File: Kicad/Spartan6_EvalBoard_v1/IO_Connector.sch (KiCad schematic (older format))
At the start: 14 parts, among them J201 CON2X45

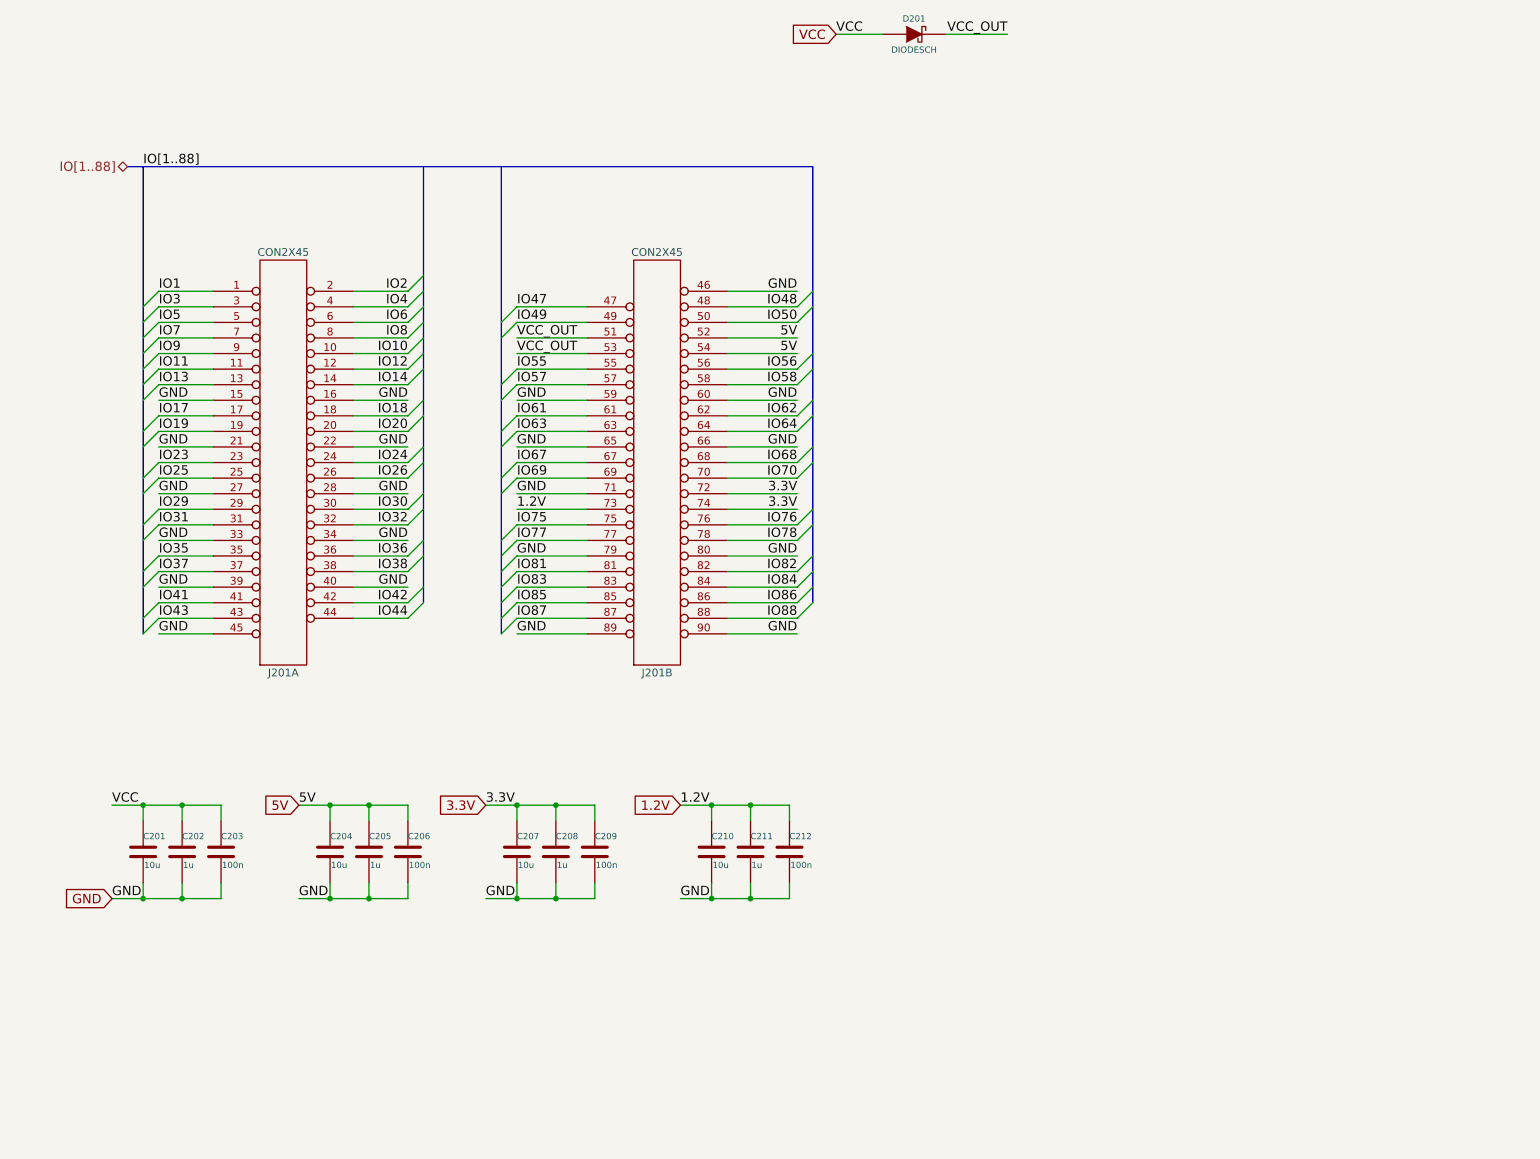
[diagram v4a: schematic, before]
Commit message: Layout completed, just need to run DRC.
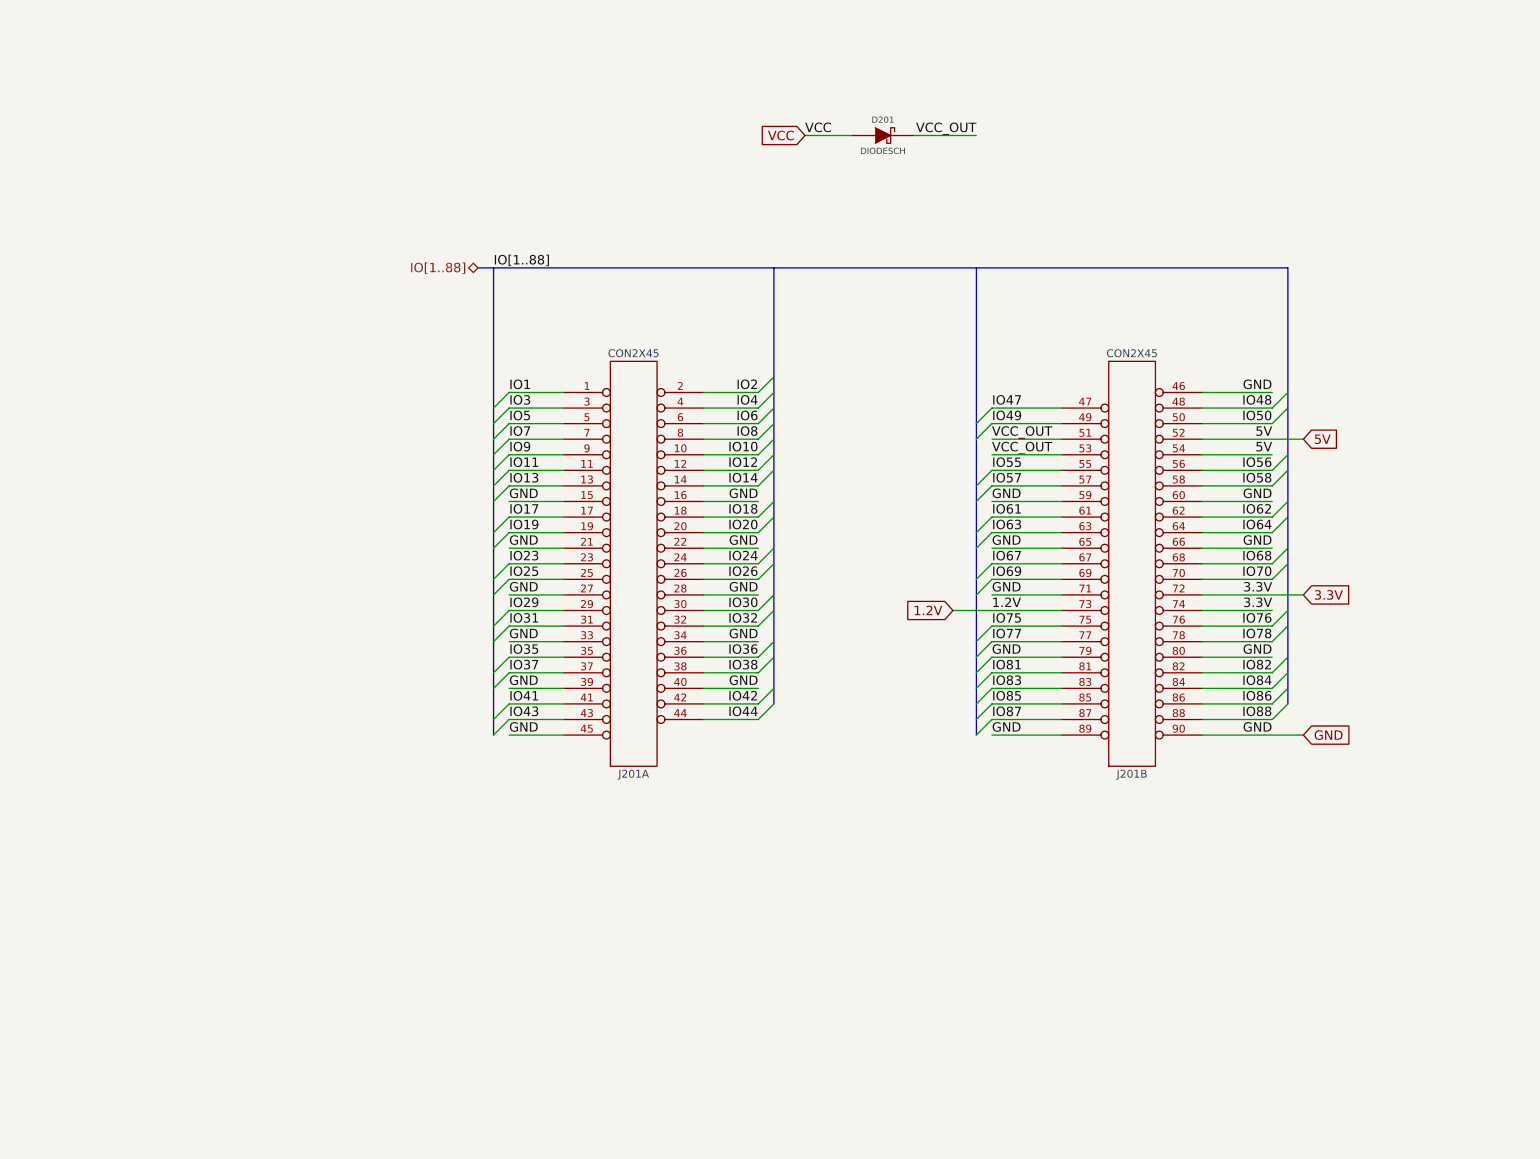
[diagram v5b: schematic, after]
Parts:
- removed C201, C204, C207, C210: 10u, Capacitors_SMD.pretty:C_0603, symbol C
- removed C202, C205, C208, C211: 1u, Capacitors_SMD.pretty:C_0402, symbol C
- removed C203, C206, C209, C212: 100n, Capacitors_SMD.pretty:C_0402, symbol C
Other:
- moved on the sheet: D201, J201A, J201B
